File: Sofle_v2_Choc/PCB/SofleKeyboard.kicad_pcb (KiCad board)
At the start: 2 copper layers, 143.4 x 111.8 mm, 84 parts, among them J2 4PIN, J3 OLED, P1 i2c_pin, P2 i2c_pin, SW1 SW_PUSH_LED, SW10 SW_PUSH_LED, SW11 SW_PUSH_LED, SW12 SW_PUSH_LED, SW13 SW_PUSH_LED, SW14 SW_PUSH_LED, SW15 SW_PUSH_LED, SW16 SW_PUSH_LED, SW17 SW_PUSH_LED, SW18 SW_PUSH_LED, SW19 SW_PUSH_LED, SW2 SW_PUSH_LED, SW20 SW_PUSH_LED, SW21 SW_PUSH_LED, SW22 SW_PUSH_LED, SW23 SW_PUSH_LED, SW24 SW_PUSH_LED, SW25 Rotary_Encoder_Switch, SW26 SW_PUSH_LED, SW27 SW_PUSH_LED, SW28 SW_PUSH_LED, SW29 SW_PUSH_LED, SW3 SW_PUSH_LED, SW30 SW_PUSH_LED, SW4 SW_PUSH_LED, SW5 SW_PUSH_LED, SW6 SW_PUSH_LED, SW7 SW_PUSH_LED, SW8 SW_PUSH_LED, SW9 SW_PUSH_LED, U1 ProMicro

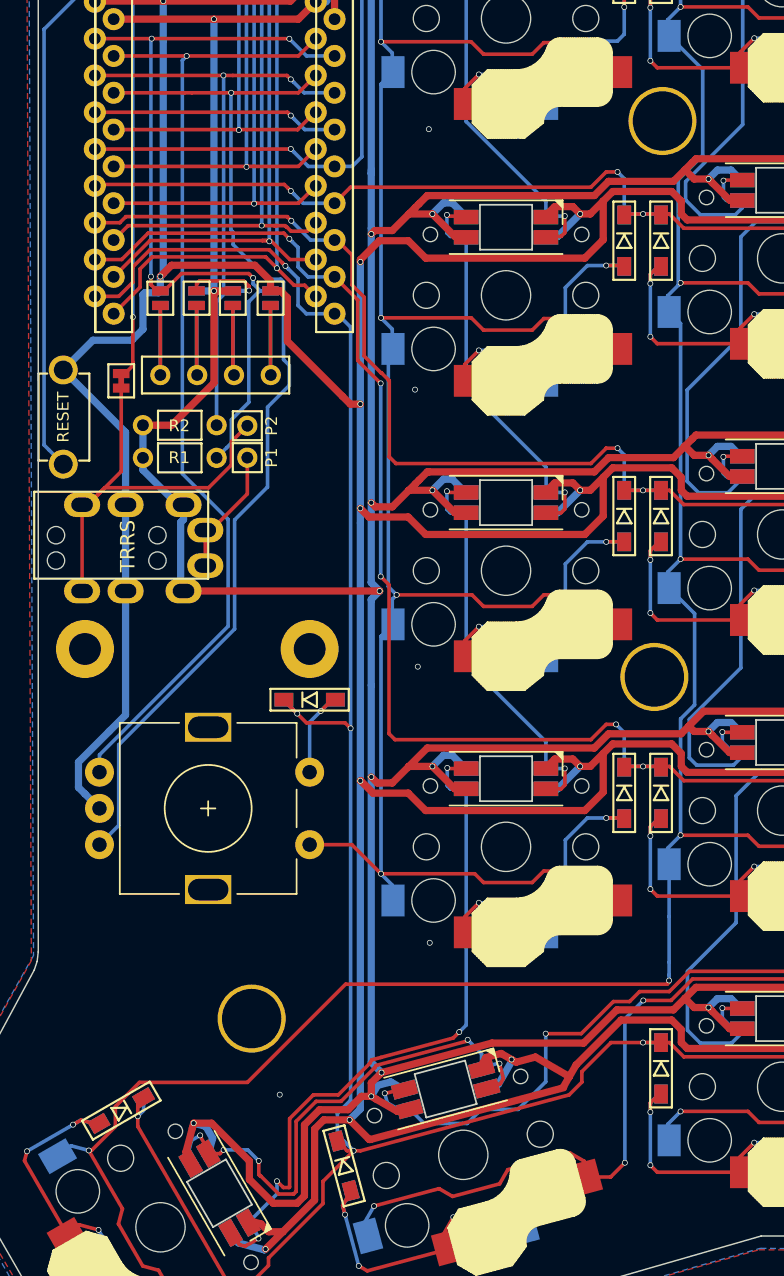
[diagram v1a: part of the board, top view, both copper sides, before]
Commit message: Move mounting holes, clean up a couple traces
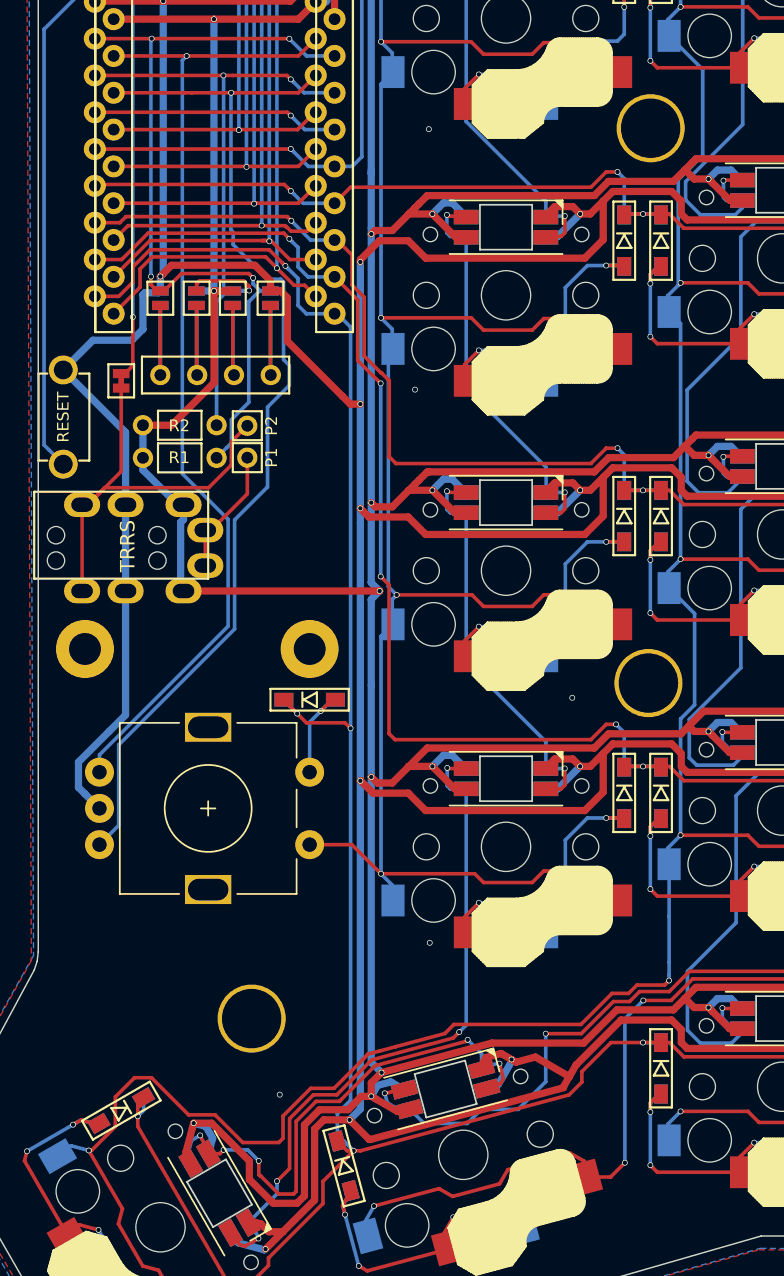
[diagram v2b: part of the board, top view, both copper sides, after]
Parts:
- moved TH3 0.96 mm to (130.5, 57.6)
- moved TH5 0.59 mm to (130.4, 95.9)
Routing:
- net col4: track 284.0 -> 288.6 mm
- net Net-(SW19-Pad2): track 48.2 -> 47.0 mm

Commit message: rename lib from SofleRGB to SofleChoc
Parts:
- SW1, SW10, SW11, SW12, SW13, SW14, SW15, SW16, SW17, SW18, SW19, SW2, SW20, SW21, SW22, SW23, SW24, SW26, SW27, SW28, SW29, SW3, SW30, SW4, SW5, SW6, SW7, SW8, SW9: footprint SofleRGB:Choc_Hotswap_SK6812MiniE -> SofleChoc:Choc_Hotswap_SK6812MiniE
